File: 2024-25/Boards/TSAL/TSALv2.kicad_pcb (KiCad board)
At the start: 2 copper layers, 87.6 x 36.8 mm, 22 parts, among them J1 043045-0412, Q1 BS250P, Q2 BS170, Q3 UJ3N120035K3S, Q4 BS170, U1 H11L1M

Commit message: Add files via upload
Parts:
- removed D10, D3, D4, D5, D6, D7, D8, D9: BZT52-B5V6X, Diode_SMD:D_SOD-123
- removed Q2: BS170, Package_TO_SOT_THT:TO-92
- added C1: 0.1uF, Capacitor_SMD:C_0805_2012Metric_Pad1.18x1.45mm_HandSolder, F.Cu at (180.9, 104.0)
- added C2: 100uF, Capacitor_SMD:C_0805_2012Metric_Pad1.18x1.45mm_HandSolder, F.Cu at (180.9, 106.4)
- added C3: 1uF, Capacitor_SMD:C_0805_2012Metric_Pad1.18x1.45mm_HandSolder, F.Cu at (180.8, 95.8)
- added R4: 1k, Resistor_SMD:R_0805_2012Metric_Pad1.20x1.40mm_HandSolder, F.Cu at (180.5, 91.2)
- added R5: 100, Resistor_SMD:R_0805_2012Metric_Pad1.20x1.40mm_HandSolder, F.Cu at (181.0, 108.8)
- added R7: 3k, Resistor_SMD:R_0805_2012Metric_Pad1.20x1.40mm_HandSolder, F.Cu at (187.3, 101.8)
- added R8: 10k, Resistor_SMD:R_0805_2012Metric_Pad1.20x1.40mm_HandSolder, F.Cu at (171.2, 101.0)
- added U2: NE555D, Package_SO:SOIC-8_3.9x4.9mm_P1.27mm, F.Cu at (180.2, 100.0)
- D2: value BZT52-B5V6X -> BZT52C12; footprint Diode_SMD:D_SOD-123 -> Diode_SMD:D_SOD-123F
- Q1: value BS250P -> DMP2035U-7; footprint Package_TO_SOT_THT:TO-92 -> Package_TO_SOT_SMD:SOT23_DIO
- Q3: value UJ3N120035K3S -> UJ3N065080K3S
- Q4: value BS170 -> DMN2056U; footprint Package_TO_SOT_THT:TO-92 -> Package_TO_SOT_SMD:SOT-23
- R1, R2, R3, R6: footprint Resistor_THT:R_Axial_DIN0207_L6.3mm_D2.5mm_P7.62mm_Horizontal -> Resistor_SMD:R_0805_2012Metric_Pad1.20x1.40mm_HandSolder
- moved Q1 17.0 mm to (173.8, 107.8)
- moved R1 13.6 mm to (173.7, 111.6), turned to 180 degrees
- moved U1 11.8 mm to (159.0, 97.7)
- moved J1 11.7 mm to (172.0, 90.0)
- moved G*** 5.65 mm to (156.2, 108.5)
- moved R3 5.63 mm to (124.9, 113.6), turned to -90 degrees
- moved R6 4.41 mm to (130.1, 85.0)
- moved Q4 1.62 mm to (116.5, 110.0)
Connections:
- net GLV- renamed GND
- D2 pad 1: Net-(D2-K) -> /HV+
- J1 pad 3: GR- -> Light+
- J1 pad 4: RD+ -> unconnected-(J1-Pin_4-Pad4)
- Q1 pad 1: RD+ -> Net-(Q1-G)
- Q1 pad 2: Net-(Q1-G) -> GLV+
- Q1 pad 3: GLV+ -> Net-(Q1-D)
- Q4 pad 1: Net-(Q4-D) -> Net-(D1-K)
- Q4 pad 2: Net-(D1-K) -> /HV-
- Q4 pad 3: /HV- -> Net-(Q4-D)
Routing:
- net Net-(Q1-G): track 35.0 -> 11.6 mm
- net Net-(U2-THR): track 0.00 -> 20.9 mm, vias 0 -> 2
- net GR-: track 20.6 -> 0.00 mm
- net Light+: track 0.00 -> 19.7 mm, vias 0 -> 1
- net GLV+: track 27.6 -> 47.1 mm, vias 0 -> 2
- net Net-(Q1-D): track 0.00 -> 19.3 mm
- net Net-(U2-DIS): track 0.00 -> 16.9 mm
- net RD+: track 16.5 -> 0.00 mm
- net GND: track 28.2 -> 42.8 mm
- net Net-(D5-K): track 9.79 -> 0.00 mm
- net /HV-: track 75.8 -> 85.4 mm
- net Net-(Q4-D): track 68.2 -> 59.7 mm, vias 0 -> 1
- net /HV+: track 36.2 -> 43.5 mm
- net Net-(D1-K): track 29.7 -> 22.6 mm
- net Net-(D10-A): track 4.64 -> 0.00 mm
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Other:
- outline, holes or cut-outs redrawn

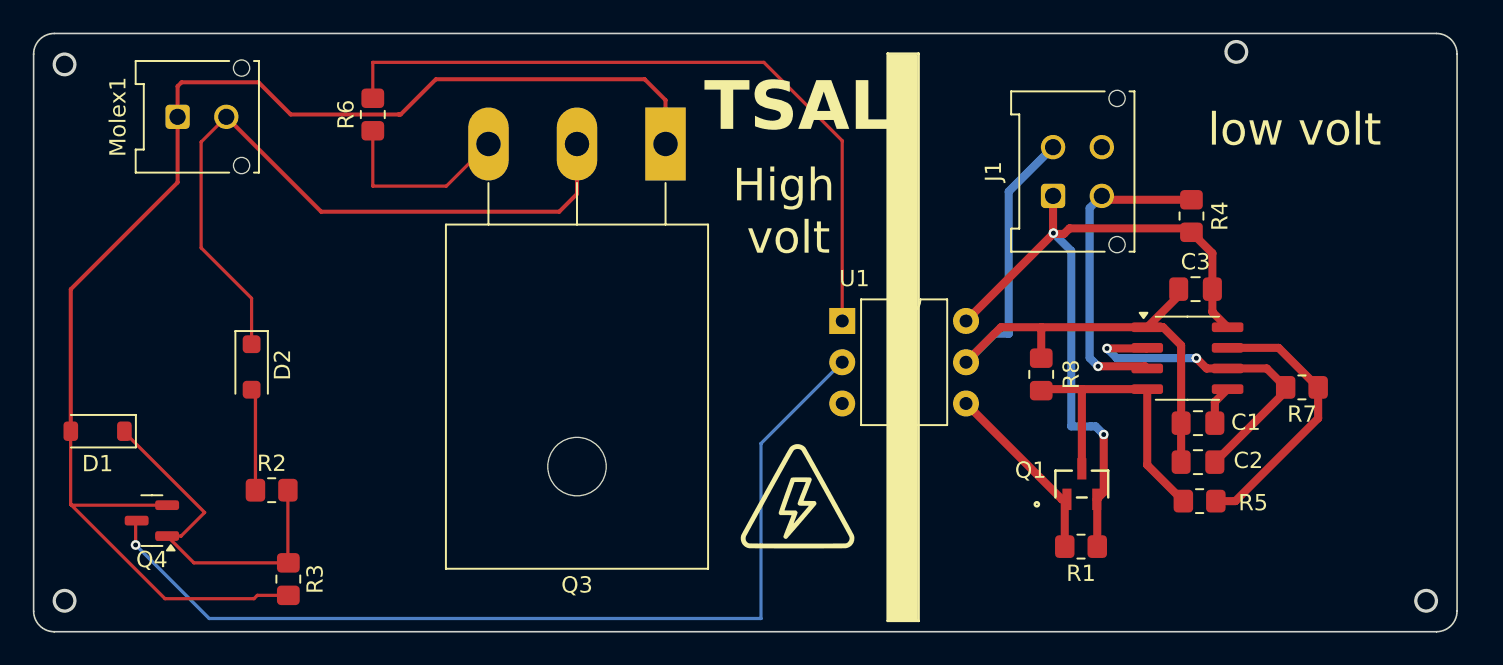
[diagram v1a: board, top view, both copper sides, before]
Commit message: split up TSAL resistors for voltage rating
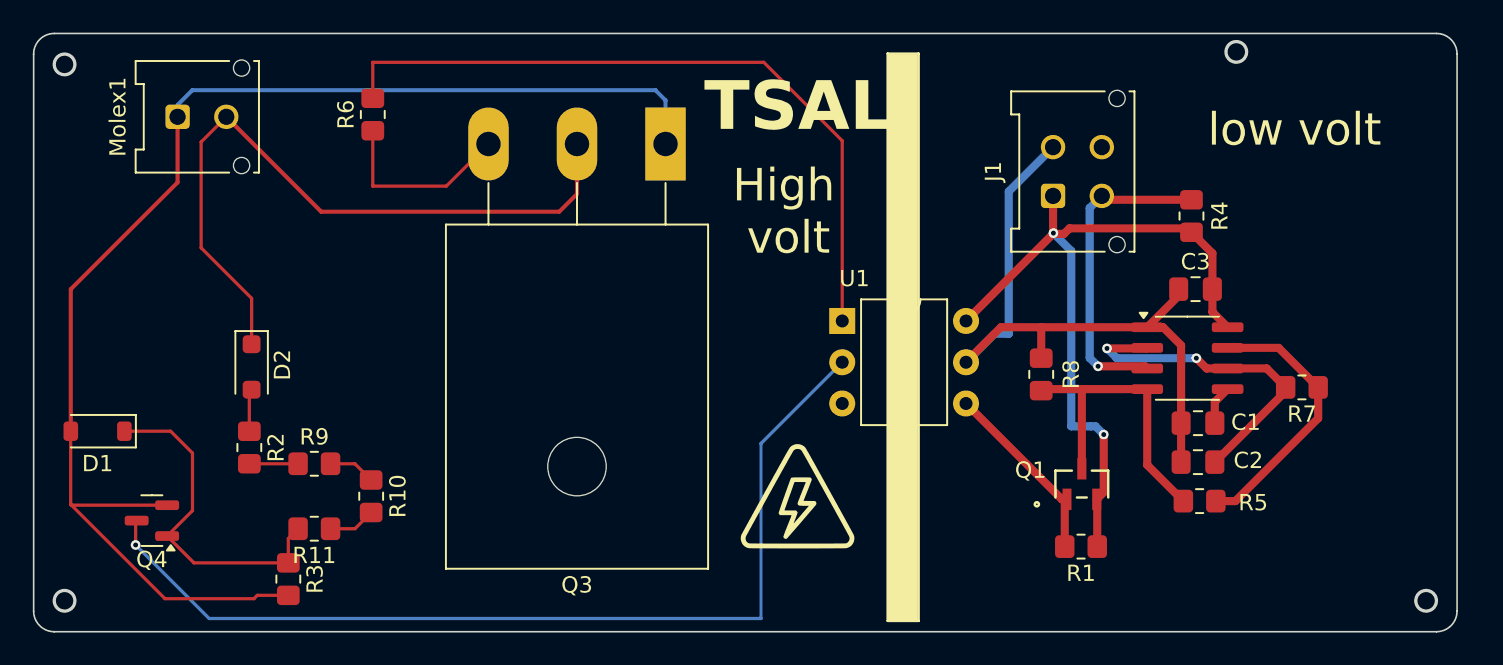
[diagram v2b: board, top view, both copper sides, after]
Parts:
- added R10: 250k, Resistor_SMD:R_0805_2012Metric_Pad1.20x1.40mm_HandSolder, F.Cu at (130.0, 108.5)
- added R11: 250k, Resistor_SMD:R_0805_2012Metric_Pad1.20x1.40mm_HandSolder, F.Cu at (126.5, 110.5)
- added R9: 250k, Resistor_SMD:R_0805_2012Metric_Pad1.20x1.40mm_HandSolder, F.Cu at (126.5, 106.5)
- R2: value PR02000201004FA100 -> 250k
- R3: value 10M -> 2M
- moved R2 2.97 mm to (122.5, 105.5), turned to -90 degrees
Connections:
- R2 pad 2: Net-(D1-K) -> Net-(R2-Pad2)
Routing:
- net Net-(D2-A): track 6.28 -> 2.95 mm
- net Net-(R2-Pad2): track 0.00 -> 3.00 mm
- net Net-(R10-Pad2): track 0.00 -> 2.91 mm
- net Net-(R10-Pad1): track 0.00 -> 2.91 mm
- net /HV-: track 85.4 -> 82.5 mm
- net Net-(D1-K): track 22.6 -> 21.4 mm

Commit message: updated resistors to be smd on VIL and added fuses and mounting holes to TSAL
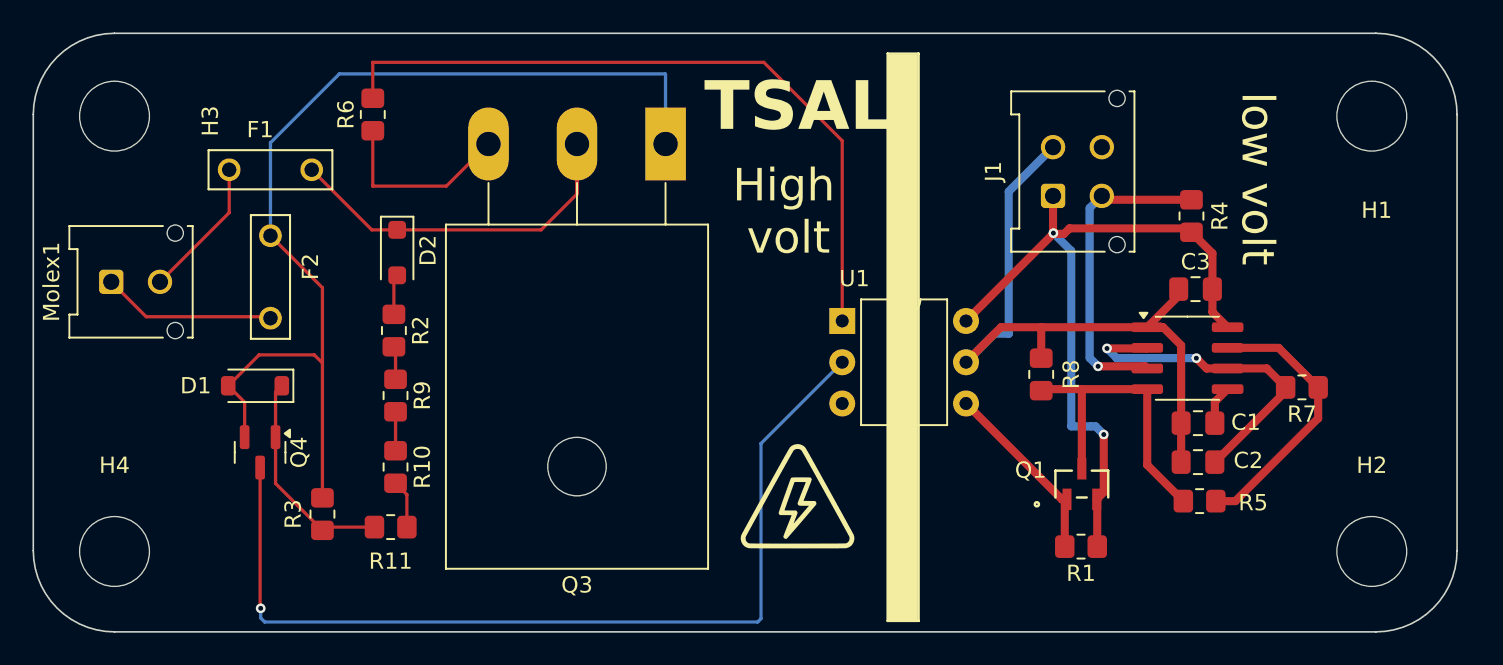
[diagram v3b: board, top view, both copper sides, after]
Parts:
- added F1: 750mA, Library:FUSE_BK_PCS, F.Cu at (123.8, 88.4)
- added F2: 750mA, Library:FUSE_BK_PCS, F.Cu at (123.8, 95.0)
- added H1: MountingHole, MountingHole:MountingHole_4.3mm_M4, F.Cu at (191.6, 85.1)
- added H2: MountingHole, MountingHole:MountingHole_4.3mm_M4, F.Cu at (191.6, 111.9)
- added H3: MountingHole, MountingHole:MountingHole_4.3mm_M4, F.Cu at (114.2, 85.1)
- added H4: MountingHole, MountingHole:MountingHole_4.3mm_M4, F.Cu at (114.2, 111.9)
- D1: value BZT52-B12_R1_00001 -> BZT52C12
- D2: value BZT52C12 -> BZT52C51
- moved R2 11.4 mm to (131.4, 98.3)
- moved D2 11.4 mm to (131.6, 93.5)
- moved Molex1 10.9 mm to (114.0, 95.3)
- moved D1 10.1 mm to (122.8, 101.7)
- moved Q4 7.88 mm to (123.2, 105.8), turned to -90 degrees
- moved R9 6.53 mm to (131.5, 102.3), turned to -90 degrees
- moved R11 4.70 mm to (131.2, 110.4)
- moved R3 4.52 mm to (127.0, 109.6), turned to 90 degrees
- moved R10 2.34 mm to (131.5, 106.7)
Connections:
- D2 pad 1: /HV+ -> Net-(D2-K)
- Molex1 pad 1: /HV- -> Net-(Molex1-Pin_1)
- Q3 pad 2: /HV+ -> Net-(D2-K)
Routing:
- net /HV+: track 43.5 -> 8.66 mm
- net Net-(D2-K): track 0.00 -> 21.9 mm
- net /HV-: track 82.5 -> 64.2 mm
- net Net-(Molex1-Pin_1): track 0.00 -> 10.7 mm
- net Net-(D1-K): track 21.4 -> 13.5 mm
- net Net-(Q4-D): track 59.7 -> 58.1 mm
- net Net-(R2-Pad2): track 3.00 -> 2.04 mm
- net Net-(R10-Pad1): track 2.91 -> 2.40 mm
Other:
- outline, holes or cut-outs redrawn

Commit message: updated names of parts
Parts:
- R6: value 5500 -> 5.5k
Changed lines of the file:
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@@
 			)
 		)
-		(property "Value" "5500"
+		(property "Value" "5.5k"
 			(at 0 1.65 90)
 			(layer "F.Fab")

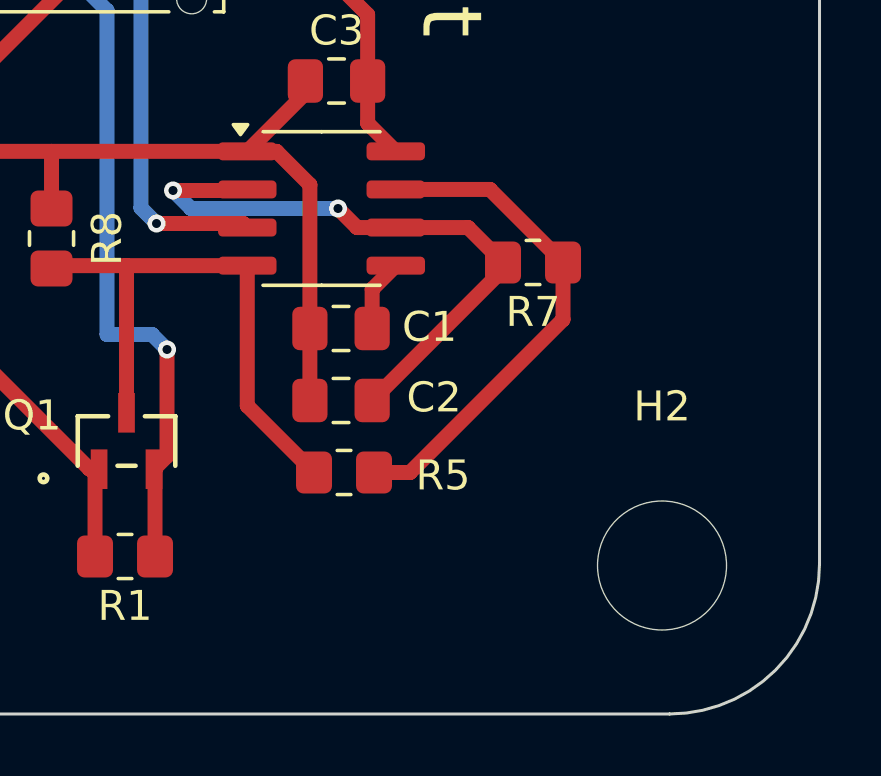
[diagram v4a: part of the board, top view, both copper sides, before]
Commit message: fixed up part names and added dnps
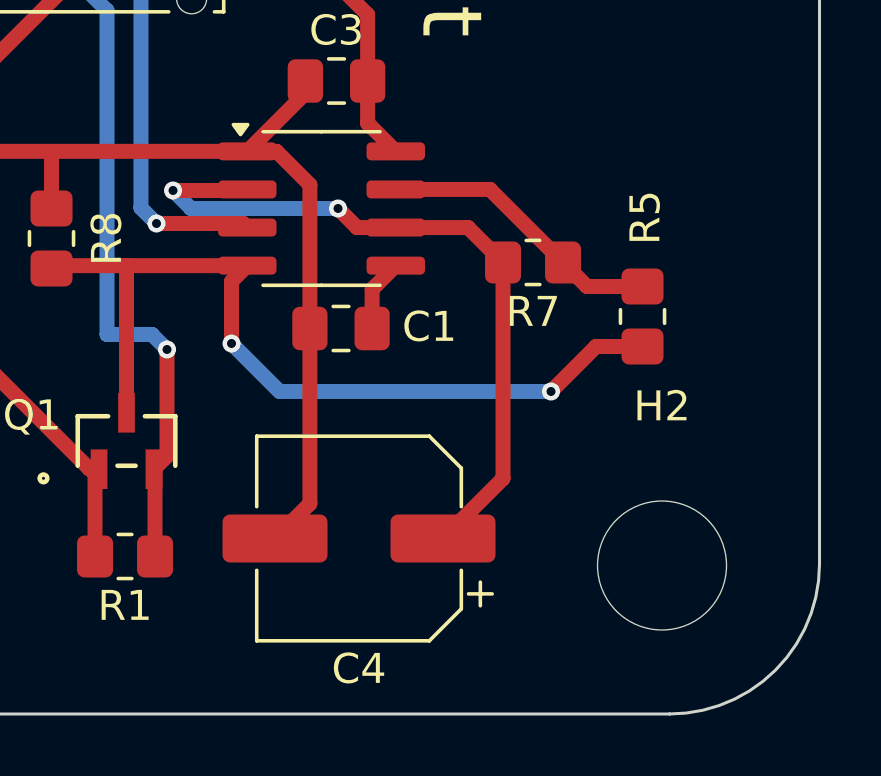
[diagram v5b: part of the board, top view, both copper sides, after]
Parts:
- removed C2: 100uF, Capacitor_SMD:C_0805_2012Metric_Pad1.18x1.45mm_HandSolder
- added C4: 100uF, Capacitor_SMD:CP_Elec_6.3x5.4, F.Cu at (181.5, 111.0)
- R10, R11, R2, R9: value 250k -> 240k
- R6: value 5.5k -> 5.6k
- moved R5 11.2 mm to (190.9, 103.6), turned to 90 degrees
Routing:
- net Net-(Q1-D): track 19.3 -> 29.3 mm, vias 0 -> 2
- net Net-(U2-DIS): track 16.9 -> 9.56 mm
- net GND: track 42.8 -> 47.9 mm
- net Net-(U2-THR): track 20.9 -> 24.9 mm
